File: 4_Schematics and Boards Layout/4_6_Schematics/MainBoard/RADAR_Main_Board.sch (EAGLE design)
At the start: 825 parts, among them IC1 AT93C46A-10SQ-2.7, J1 142-0731-211, J18 142-0731-211, J19 CJT-T-P-HH-ST-TH1, J20 142-0731-211, J21 CJT-T-P-HH-ST-TH1, J22 142-0731-211, J23 142-0731-211, J24 142-0731-211, J25 142-0731-211, J26 142-0731-211, J27 142-0731-211, J28 142-0731-211, J29 142-0731-211, J30 142-0731-211, J31 142-0731-211, J32 142-0731-211, J33 142-0731-211, J34 142-0731-211, J35 142-0731-211, J36 142-0731-211, J37 142-0731-211, J38 142-0731-211, J39 142-0731-211, J40 142-0731-211, J41 142-0731-211, J42 142-0731-211, J43 142-0731-211, J44 142-0731-211, J45 142-0731-211, J46 142-0731-211, J47 142-0731-211, J48 142-0731-211, J49 142-0731-211, J50 142-0731-211, J51 142-0731-211, J52 142-0731-211, J53 142-0731-211, J54 142-0731-211, J55 142-0731-211, J56 142-0731-211, J57 142-0731-211, J58 142-0731-211, J59 142-0731-211, U1 AD9484BCPZ-500, U10 ADS7830IPWR, U11 INA241A4IDGKRDGK0008A-MFG, U13 LTC5552IUDBTRMPBF, U14 SZMMSZ5232BT1G, U15 SZMMSZ5232BT1G, U16 EP4RKU+, U17 SZMMSZ5232BT1G, U2 STM32F746ZGT7, U3 AD9708AR, U37 SZMMSZ5232BT1G, U38 SZMMSZ5232BT1G, U39 SZMMSZ5232BT1G, U4 AD8352ACPZ-R7, U40 SZMMSZ5232BT1G, U41 SZMMSZ5232BT1G, U42 XC7A50T-2FTG256I, U43 SZMMSZ5232BT1G, U44 SZMMSZ5232BT1G, U45 SZMMSZ5232BT1G, U46 SZMMSZ5232BT1G, U47 SZMMSZ5232BT1G, U48 SZMMSZ5232BT1G, U49 SZMMSZ5232BT1G, U5 LTC5552IUDBTRMPBF, U50 SZMMSZ5232BT1G, U51 SZMMSZ5232BT1G, U52 SZMMSZ5232BT1G, U53 SZMMSZ5232BT1G, U54 SZMMSZ5232BT1G, U55 SZMMSZ5232BT1G, U56 SZMMSZ5232BT1G, U57 SZMMSZ5232BT1G, U58 SZMMSZ5232BT1G, U59 SZMMSZ5232BT1G, U6 FT2232HQ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

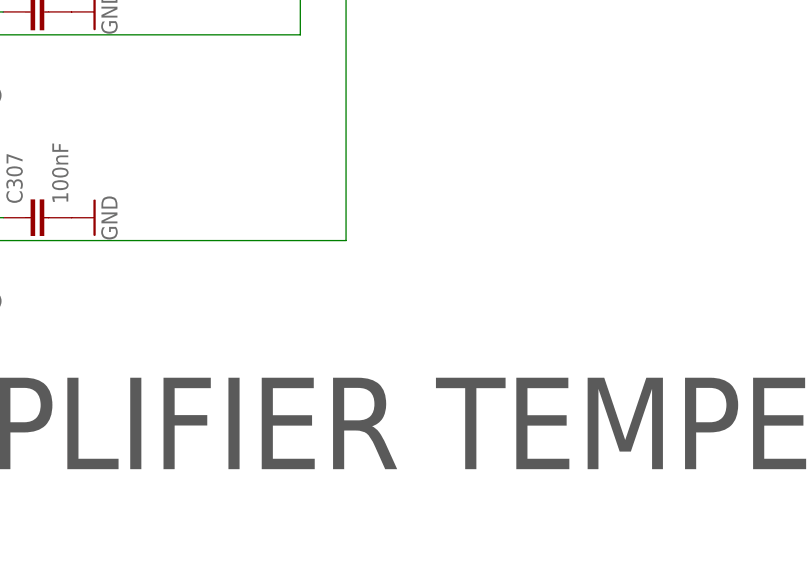
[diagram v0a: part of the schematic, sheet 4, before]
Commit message: feat(hw): a working AD9484 serial port, and the part-number sweep (#14 #22)
#14 the AD9484's serial port could not be used at all
  CSB was tied to a supply rail - the datasheet names that as the way to disable the SPI -
  SCLK/DFS was decided by solder jumper SJ1, and SDIO was not connected.  The pins are
  DRVDD-referenced 1.8 V logic: the absolute maximum is "SDIO/DCS to DRGND: -0.3 V to
  DRVDD + 0.2 V", i.e. 2.0 V, and the equivalent input circuits show CSB and SDIO referenced to
  DRVDD.  They cannot be driven from a 3.3 V bank, and the FPGA's 1.8 V bank has one free pin,
  so a translator is required - and the repo already had the part, U90/U91 from the flash work.

  U92 (TXS0104EPWR) sits between the ADC and the MCU: VCCA on the ADC's own digital supply,
  VCCB on +3V3, OE pulled up to VCCA, and the three signals on PC10/PC11/PC13.  The master is
  the MCU rather than the FPGA - all three parts are on the main board, the MCU owns bring-up,
  and the port is slow (tCLK >= 40 ns), so bit-banging is ample and no RTL is needed.

  Two deliberate choices, both safe at power-up: SCLK/DFS idles LOW, because the datasheet's
  default is offset binary and nothing in the FPGA converts two's complement - SJ1 as built
  strapped it to a 1.8 V rail, i.e. two's complement, which would put the whole capture half a
  scale out; and CSB idles HIGH through the translator's internal pull-up, so the ADC stays in
  strapped mode until the firmware talks.

  AD9484_SPI.{h,c} implement the 16-bit instruction + 8-bit data frame from the datasheet's
  serial timing, with readback turnaround, and use the registers the memory map names: 0x0D
  TEST_IO, 0x14 OUTPUT_MODE (00 = offset binary, 01 = two's complement), 0x19/0x1A user
  pattern.  Bring-up selects offset binary explicitly rather than trusting the strap, reads
  back 0x2A (OVR_CONFIG, default 0x01) and reports both, so a dead interface shows as a wrong
  value in telemetry instead of as a silently missing feature.

#22 the pa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
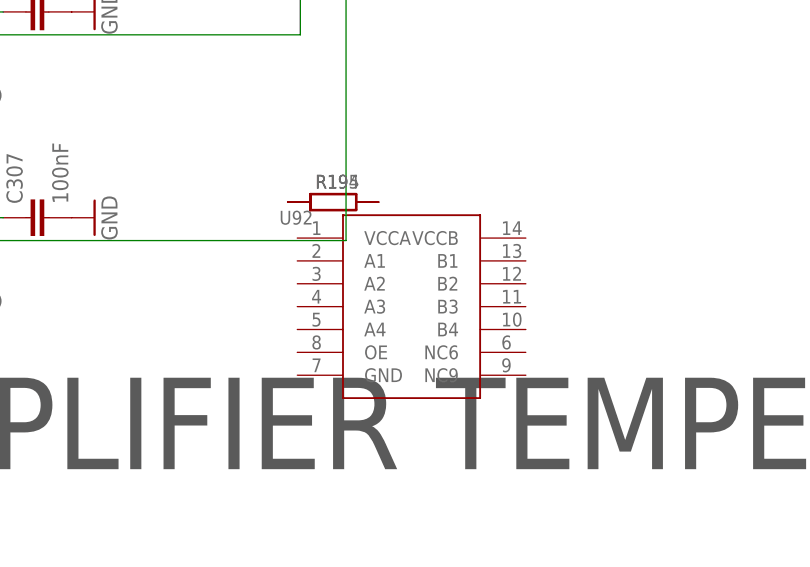
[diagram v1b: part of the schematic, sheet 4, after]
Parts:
- added R194: 10k, rcl:R-EU_R0201
- added R195: 4.7k, rcl:R-EU_R0201
- added U92: TXS0104EPWR, My_Library_RADAR:TXS0104EPWR
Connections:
- removed net N$6: SJ1.2, U1.SCLK/DFS
- new net ADC_SPI_CSB: U1.CSB, U92.A1
- new net ADC_SPI_SCLK: R195.1, SJ1.2, U1.SCLK/DFS, U92.A2
- new net ADC_SPI_SDIO: U1.SDIO, U92.A3
- new net MCU_ADC_CSB: U2A.PC10, U92.B1
- new net MCU_ADC_SCLK: U2A.PC11, U92.B2
- new net MCU_ADC_SDIO: U2A.PC13, U92.B3
- new net N$U92_OE: R194.1, U92.OE
- net +1V8_CLOCK_F: no longer SJ1.3, U1.CSB
- net +1V8_FPGA: now also R194.2, U92.VCCA
- net +3V3: now also U92.VCCB
- net GND: now also R195.2, SJ1.3, U92.GND
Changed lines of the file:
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@@
 </class>
 </classes>
-<parts>
+<parts><part name="R195" library="rcl" deviceset="R-EU_" device="R0201" value="4.7k"/><part name="R194" library="rcl" deviceset="R-EU_" device="R0201" value="10k"/><part name="U92" library="My_Library_RADAR" deviceset="TXS0104EPWR" device=""/>
 <part name="U2" library="My_Library" deviceset="STM32F746ZGT7" device=""/>
 <part name="XTAL1" library="My_Library" deviceset="NX3225GD-8MHZ-STD-CRA-3" device=""/>
@@
 <busses>
 </busses>
-<nets><net name="FPGA_STROBE_ACK" class="0"><segment><pinref part="U42" gate="G$3" pin="IO_L10N_T1_AD11N_15"/><pinref part="U2" gate="A" pin="PC3"/></segment></net><net name="PG_2V5_FPGA" class="0"><segment><pinref part="X27" gate="-1" pin="S"/><pinref part="U2" gate="A" pin="PC2"/></segment></net><net name="PG_3V3_XO" class="0"><segment><pinref part="X26" gate="-1" pin="S"/><pinref part="U2" gate="A" pin="PC1"/></segment></net><net name="PG_3V3_ADTR" class="0"><segment><pinref part="X25" gate="-1" pin="S"/><pinref part="U2" gate="A" pin="PC0"/></segment></net><net name="N$U91_OE" class="0"><segment><pinref part="U91" gate="G$1" pin="OE"/><pinref part="R177" gate="G$1" pin="1"/></segment></net><net name="N$U90_OE" class="0"><segment><pinref part="U90" gate="G$1" pin="OE"/><pinref part="R176" gate="G$1" pin="1"/></segment></net><net name="+2V5_FPGA" class="0"><segment><pinref part="U90" gate="G$1" pin="VCCA"/><pinref part="U91" gate="G$1" pin="VCCA"/><pinref part="R176" gate="G$1" pin="2"/><pinref part="R177" gate="G$1" pin="2"/><pinref part="C354" gate="G$1" pin="1"/><pinref part="C355" gate="G$1" pin="1"/><pinref part="C358" gate="G$1" pin="1"/><pinref part="C359" gate="G$1" pin="1"/><pinref part="X57" gate="-1" pin="S"/><pinref part="U42" gate="G$2" pin="VCCO_14"/></segment></net><net name="FLASH_NRST_F" class="0"><segment><pinref part="U9" gate="A" pin="RESET"/><pinref part="U91" gate="G$1" pin="B2"/></segment></net><net name="FLASH_NCS_F" class="0"><segment><pinref part="U9" gate="A" pin="S"/><pinref part="U91" gate="G$1" pin="B1"/></segment></net><net name="FLASH_DQ3_F" class="0"><segment><pinref part="U9" gate="A" pin="DQ3/HOLD"/><pinref part="U90" gate="G$1" pin="B4"/></segment></net><net name="FLASH_DQ2_F" class="0"><segment><pinref part="U9" gate="A" pin="W/DQ2"/><pinref part="U90" gate="G$1" pin="B3"/></segment></net><net name="FLASH_DQ1_F" class="0"><segment><pinref part="U9" gate="A" pin="DQ1"/><pinref part="U90" gate="G$1" pin="B2"/></segment></net><net name="FLASH_DQ0_F" class="0"><segment><pinref part="U9" gate="A" pin="DQ0"/><pinref part="U90" gate="G$1" pin="B1"/></segment></net>
+<nets><net name="MCU_ADC_SDIO" class="0"><segment><pinref part="U2" gate="A" pin="PC13"/><pinref part="U92" gate="G$1" pin="B3"/></segment></net><net name="MCU_ADC_SCLK" class="0"><segment><pinref part="U2" gate="A" pin="PC11"/><pinref part="U92" gate="G$1" pin="B2"/></segment></net><net name="MCU_ADC_CSB" class="0"><segment><pinref part="U2" gate="A" pin="PC10"/><pinref part="U92" gate="G$1" pin="B1"/></segment></net><net name="ADC_SPI_SDIO" class="0"><segment><pinref part="U1" gate="A" pin="SDIO"/><pinref part="U92" gate="G$1" pin="A3"/></segment></net><net name="ADC_SPI_SCLK" class="0"><segment><pinref part="U1" gate="A" pin="SCLK/DFS"/><pinref part="U92" gate="G$1" pin="A2"/><pinref part="R195" gate="G$1" pin="1"/><pinref part="SJ1" gate="G$1" pin="2"/></segment></net><net name="ADC_SPI_CSB" class="0"><segment><pinref part="U1" gate="A" pin="CSB"/><pinref part="U92" gate="G$1" pin="A1"/></segment></net><net name="N$U92_OE" class="0"><segment><pinref part="U92" gate="G$1" pin="OE"/><pinref part="R194" gate="G$1" pin="1"/></segment></net><net name="FPGA_STROBE_ACK" class="0"><segment><pinref part="U42" gate="G$3" pin="IO_L10N_T1_AD11N_15"/><pinref part="U2" gate="A" pin="PC3"/></segment></net><net name="PG_2V5_FPGA" class="0"><segment><pinref part="X27" gate="-1" pin="S"/><pinref part="U2" gate="A" pin="PC2"/></segment></net><net name="PG_3V3_XO" class="0"><segment><pinref part="X26" gate="-1" pin="S"/><pinref part="U2" gate="A" pin="PC1"/></segment></net><net name="PG_3V3_ADTR" class="0"><segment><pinref part="X25" gate="-1" pin="S"/><pinref part="U2" gate="A" pin="PC0"/></segment></net><net name="N$U91_OE" class="0"><segment><pinref part="U91" gate="G$1" pin="OE"/><pinref part="R177" gate="G$1" pin="1"/></segment></net><net name="N$U90_OE" class="0"><segment><pinref part="U90" gate="G$1" pin="OE"/><pinref part="R176" gate="G$1" pin="1"/></segment></net><net name="+2V5_FPGA" class="0"><segment><pinref part="U90" gate="G$1" pin="VCCA"/><pinref part="U91" gate="G$1" pin="VCCA"/><pinref part="R176" gate="G$1" pin="2"/><pinref part="R177" gate="G$1" pin="2"/><pinref part="C354" gate="G$1" pin="1"/><pinref part="C355" gate="G$1" pin="1"/><pinref part="C358" gate="G$1" pin="1"/><pinref part="C359" gate="G$1" pin="1"/><pinref part="X57" gate="-1" pin="S"/><pinref part="U42" gate="G$2" pin="VCCO_14"/></segment></net><net name="FLASH_NRST_F" class="0"><segment><pinref part="U9" gate="A" pin="RESET"/><pinref part="U91" gate="G$1" pin="B2"/></segment></net><net name="FLASH_NCS_F" class="0"><segment><pinref part="U9" gate="A" pin="S"/><pinref part="U91" gate="G$1" pin="B1"/></segment></net><net name="FLASH_DQ3_F" class="0"><segment><pinref part="U9" gate="A" pin="DQ3/HOLD"/><pinref part="U90" gate="G$1" pin="B4"/></segment></net><net name="FLASH_DQ2_F" class="0"><segment><pinref part="U9" gate="A" pin="W/DQ2"/><pinref part="U90" gate="G$1" pin="B3"/></segment></net><net name="FLASH_DQ1_F" class="0"><segment><pinref part="U9" gate="A" pin="DQ1"/><pinref part="U90" gate="G$1" pin="B2"/></segment></net><net name="FLASH_DQ0_F" class="0"><segment><pinref part="U9" gate="A" pin="DQ0"/><pinref part="U90" gate="G$1" pin="B1"/></segment></net>
 <net name="+3V3" class="0">
 <segment>
@@
 <wire x1="203.2" y1="175.26" x2="200.66" y2="175.26" width="0.1524" layer="91"/>
 <label x="195.58" y="175.26" size="1.778" layer="95"/>
-</segment>
+<pinref part="U92" gate="G$1" pin="VCCB"/></segment>
 </net>
 <net name="GND" class="0">
@@
 <pinref part="X22" gate="-2" pin="S"/>
 <pinref part="GND1079" gate="1" pin="GND"/>
-<pinref part="U90" gate="G$1" pin="GND"/><pinref part="U91" gate="G$1" pin="GND"/><pinref part="C354" gate="G$1" pin="2"/><pinref part="C355" gate="G$1" pin="2"/><pinref part="C356" gate="G$1" pin="2"/><pinref part="C357" gate="G$1" pin="2"/><pinref part="C358" gate="G$1" pin="2"/><pinref part="C359" gate="G$1" pin="2"/><pinref part="X57" gate="-2" pin="S"/><pinref part="X25" gate="-2" pin="S"/><pinref part="X26" gate="-2" pin="S"/><pinref part="X27" gate="-2" pin="S"/><pinref part="X6" gate="-3" pin="S"/><pinref part="X19" gate="-3" pin="S"/><pinref part="X15" gate="-3" pin="S"/><pinref part="X13" gate="-3" pin="S"/><pinref part="X11" gate="-3" pin="S"/><pinref part="X22" gate="-3" pin="S"/><pinref part="X14" gate="-3" pin="S"/><pinref part="X14" gate="-4" pin="S"/><pinref part="X5" gate="-3" pin="S"/><pinref part="X5" gate="-4" pin="S"/><pinref part="X7" gate="-3" pin="S"/><pinref part="X7" gate="-4" pin="S"/></segment>
+<pinref part="U90" gate="G$1" pin="GND"/><pinref part="U91" gate="G$1" pin="GND"/><pinref part="C354" gate="G$1" pin="2"/><pinref part="C355" gate="G$1" pin="2"/><pinref part="C356" gate="G$1" pin="2"/><pinref part="C357" gate="G$1" pin="2"/><pinref part="C358" gate="G$1" pin="2"/><pinref part="C359" gate="G$1" pin="2"/><pinref part="X57" gate="-2" pin="S"/><pinref part="X25" gate="-2" pin="S"/><pinref part="X26" gate="-2" pin="S"/><pinref part="X27" gate="-2" pin="S"/><pinref part="X6" gate="-3" pin="S"/><pinref part="X19" gate="-3" pin="S"/><pinref part="X15" gate="-3" pin="S"/><pinref part="X13" gate="-3" pin="S"/><pinref part="X11" gate="-3" pin="S"/><pinref part="X22" gate="-3" pin="S"/><pinref part="X14" gate="-3" pin="S"/><pinref part="X14" gate="-4" pin="S"/><pinref part="X5" gate="-3" pin="S"/><pinref part="X5" gate="-4" pin="S"/><pinref part="X7" gate="-3" pin="S"/><pinref part="X7" gate="-4" pin="S"/><pinref part="U92" gate="G$1" pin="GND"/><pinref part="R195" gate="G$1" pin="2"/><pinref part="SJ1" gate="G$1" pin="3"/></segment>
 </net>
 <net name="+1V8_FPGA" class="0">
@@
 <wire x1="121.92" y1="248.92" x2="119.38" y2="248.92" width="0.1524" layer="91"/>
 <label x="106.68" y="248.92" size="1.778" layer="95"/>
-</segment>
+<pinref part="U92" gate="G$1" pin="VCCA"/><pinref part="R194" gate="G$1" pin="2"/></segment>
 </net>
 <net name="+1V0_FPGA" class="0">
@@
 <net name="+1V8_CLOCK_F" class="0">
 <segment>
-<pinref part="U1" gate="A" pin="CSB"/>
 <wire x1="73.66" y1="83.82" x2="63.5" y2="83.82" width="0.1524" layer="91"/>
 <label x="58.42" y="83.82" size="1.778" layer="95"/>
@@
 </segment>
 <segment>
-<pinref part="SJ1" gate="G$1" pin="3"/>
 <wire x1="43.18" y1="91.44" x2="43.18" y2="93.98" width="0.1524" layer="91"/>
 <label x="43.18" y="93.98" size="1.778" layer="95" rot="R90"/>
@@
 <net name="N$6" class="0">
 <segment>
-<pinref part="U1" gate="A" pin="SCLK/DFS"/>
-<pinref part="SJ1" gate="G$1" pin="2"/>
 <wire x1="73.66" y1="86.36" x2="48.26" y2="86.36" width="0.1524" layer="91"/>
 </segment>
@@
 <text x="55.88" y="274.32" size="10.16" layer="97">RF POWER AMPLIFIER TEMPERATURE SENSING</text>
 </plain>
-<instances>
+<instances><instance part="R195" gate="G$1" x="184" y="304" smashed="yes"><attribute name="NAME" x="182" y="305.5" size="1.524" layer="95"/></instance><instance part="R194" gate="G$1" x="184" y="304" smashed="yes"><attribute name="NAME" x="182" y="305.5" size="1.524" layer="95"/></instance><instance part="U92" gate="G$1" x="180" y="300" smashed="yes"><attribute name="NAME" x="178" y="301.5" size="1.524" layer="95"/></instance>
 <instance part="U7" gate="A" x="53.34" y="205.74" smashed="yes">
 <attribute name="NAME" x="81.6356" y="214.8586" size="2.0828" layer="95" ratio="6" rot="SR0"/>

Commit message: feat(hw): the eight temperature channels, and a filter that meets the requirement (#5 #7)
#5 The issue said the harness had no spare position, so the sensors could not reach the MCU. The
   second half was the wrong question: the main board already carries the whole interface.

   Three ADS7830s exist and are in the BOM - U10 (0x48), U88 (0x4A), U89 (0x4B) - and the firmware
   names exactly these hadc1/hadc2/hadc3. U89's eight channels run to eight 3-pin headers (JP5,
   JP6, JP11, JP12, JP14, JP15, JP16, JP19), each bringing out +3V3_AN4_F, the channel and GND.
   The probes are therefore external, on flying leads, and belong at the PA where the temperature
   is actually wanted.

   What was missing was three things:
     * a pull-up - the channel nets carried only the header and the ADC pin, so an NTC would have
       had nothing to divide against.  Eight 10k 0201 resistors (R196-R203) now pull each channel
       up to +3V3_AN4_F, reusing the repo's own rcl/R-EU_/R0201 deviceset;
     * names - the anonymous N$ nets are now TEMP_1..TEMP_8 in U89's channel order, so the
       firmware's index maps onto the net name;
     * a firmware bug - hadc3 was read eight times per cycle and NEVER INITIALISED.  Only hadc1
       and hadc2 were.  Every Temperature_N was reading an unconfigured part.

   The conversion was wrong in two different ways as well: the bring-up read stored raw 8-bit
   codes while the loop read applied a linear *0.64705f, and neither is right for a thermistor.
   Both sites now call one reader using PA_Thermal_NtcToCelsius(), which inverts the divider and
   applies the B-equation, and returns false for an unplugged probe - which sits on the rail and
   would otherwise read as a very cold board.

   The model reproduces the design's own numbers: with a 10k pull-up equal to the probe's R25 the
   divider midpoint is exactly 25.0 degC, and ratio 0.10 lands on 95.3 degC, which is the case
   limit derived from the QPA2962's theta_JC (95.4 degC).  Th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
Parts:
- added R196, R197, R198, R199, R200, R201, R202, R203: 10k, rcl:R-EU_R0201
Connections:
- removed net N$295: JP5.2, U89.CH3
- removed net N$296: JP6.2, U89.CH4
- removed net N$297: JP19.2, U89.CH0
- removed net N$298: JP12.2, U89.CH6
- removed net N$299: JP14.2, U89.CH1
- removed net N$301: JP16.2, U89.CH7
- removed net N$306: JP11.2, U89.CH5
- removed net N$307: JP15.2, U89.CH2
- new net TEMP_1: JP19.2, R196.1, U89.CH0
- new net TEMP_2: JP14.2, R197.1, U89.CH1
- new net TEMP_3: JP15.2, R198.1, U89.CH2
- new net TEMP_4: JP5.2, R199.1, U89.CH3
- new net TEMP_5: JP6.2, R200.1, U89.CH4
- new net TEMP_6: JP11.2, R201.1, U89.CH5
- new net TEMP_7: JP12.2, R202.1, U89.CH6
- new net TEMP_8: JP16.2, R203.1, U89.CH7
- net +3V3_AN4_F: now also R196.2, R197.2, R198.2, R199.2, R200.2, R201.2, R202.2, R203.2
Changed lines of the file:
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@@
 <part name="C353" library="eagle-ltspice" deviceset="C" device="C0201" value="0.1uF"/>
 <part name="GND1099" library="supply1" deviceset="GND" device=""/>
-</parts>
+  <part name="R196" library="rcl" deviceset="R-EU_" device="R0201" value="10k"/>
+  <part name="R197" library="rcl" deviceset="R-EU_" device="R0201" value="10k"/>
+  <part name="R198" library="rcl" deviceset="R-EU_" device="R0201" value="10k"/>
+  <part name="R199" library="rcl" deviceset="R-EU_" device="R0201" value="10k"/>
+  <part name="R200" library="rcl" deviceset="R-EU_" device="R0201" value="10k"/>
+  <part name="R201" library="rcl" deviceset="R-EU_" device="R0201" value="10k"/>
+  <part name="R202" library="rcl" deviceset="R-EU_" device="R0201" value="10k"/>
+  <part name="R203" library="rcl" deviceset="R-EU_" device="R0201" value="10k"/></parts>
 <sheets>
 <sheet>
@@
 </segment>
 </net>
-<net name="N$295" class="0">
+<net name="TEMP_4" class="0">
 <segment>
 <pinref part="JP5" gate="A" pin="2"/>
@@
 <wire x1="160.02" y1="381" x2="185.42" y2="381" width="0.1524" layer="91"/>
 </segment>
-</net>
-<net name="N$296" class="0">
+        <pinref part="R199" gate="G$1" pin="1"/></net>
+<net name="TEMP_5" class="0">
 <segment>
 <pinref part="U89" gate="A" pin="CH4"/>
@@
 <pinref part="JP6" gate="A" pin="2"/>
 </segment>
-</net>
-<net name="N$298" class="0">
+        <pinref part="R200" gate="G$1" pin="1"/></net>
+<net name="TEMP_7" class="0">
 <segment>
 <wire x1="180.34" y1="322.58" x2="137.16" y2="322.58" width="0.1524" layer="91"/>
@@
 <wire x1="180.34" y1="373.38" x2="185.42" y2="373.38" width="0.1524" layer="91"/>
 </segment>
-</net>
-<net name="N$301" class="0">
+        <pinref part="R202" gate="G$1" pin="1"/></net>
+<net name="TEMP_8" class="0">
 <segment>
 <pinref part="JP16" gate="A" pin="2"/>
@@
 <wire x1="185.42" y1="299.72" x2="185.42" y2="370.84" width="0.1524" layer="91"/>
 </segment>
-</net>
-<net name="N$306" class="0">
+        <pinref part="R203" gate="G$1" pin="1"/></net>
+<net name="TEMP_6" class="0">
 <segment>
 <pinref part="JP11" gate="A" pin="2"/>
@@
 <wire x1="175.26" y1="375.92" x2="175.26" y2="345.44" width="0.1524" layer="91"/>
 </segment>
-</net>
-<net name="N$307" class="0">
+        <pinref part="R201" gate="G$1" pin="1"/></net>
+<net name="TEMP_3" class="0">
 <segment>
 <wire x1="175.26" y1="414.02" x2="137.16" y2="414.02" width="0.1524" layer="91"/>
@@
 <wire x1="175.26" y1="383.54" x2="185.42" y2="383.54" width="0.1524" layer="91"/>
 </segment>
-</net>
-<net name="N$299" class="0">
+        <pinref part="R198" gate="G$1" pin="1"/></net>
+<net name="TEMP_2" class="0">
 <segment>
 <pinref part="U89" gate="A" pin="CH1"/>
@@
 <wire x1="180.34" y1="386.08" x2="185.42" y2="386.08" width="0.1524" layer="91"/>
 </segment>
-</net>
-<net name="N$297" class="0">
+        <pinref part="R197" gate="G$1" pin="1"/></net>
+<net name="TEMP_1" class="0">
 <segment>
 <pinref part="JP19" gate="A" pin="2"/>
@@
 <wire x1="185.42" y1="459.74" x2="185.42" y2="388.62" width="0.1524" layer="91"/>
 </segment>
-</net>
+        <pinref part="R196" gate="G$1" pin="1"/></net>
 <net name="+3V3_AN3_F" class="0">
 <segment>
@@
 <wire x1="574.04" y1="327.66" x2="574.04" y2="325.12" width="0.1524" layer="91"/>
 </segment>
-</net>
+        <pinref part="R196" gate="G$1" pin="2"/>
+        <pinref part="R197" gate="G$1" pin="2"/>
+        <pinref part="R198" gate="G$1" pin="2"/>
+        <pinref part="R199" gate="G$1" pin="2"/>
+        <pinref part="R200" gate="G$1" pin="2"/>
+        <pinref part="R201" gate="G$1" pin="2"/>
+        <pinref part="R202" gate="G$1" pin="2"/>
+        <pinref part="R203" gate="G$1" pin="2"/></net>
 <net name="+3V3_AN5_F" class="0">
 <segment>
